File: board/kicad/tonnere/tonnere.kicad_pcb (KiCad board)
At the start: 6 copper layers, 256.2 x 141.3 mm, 403 parts, among them J1 PJ-325C5-G, J10 STM SWD, J12 Conn_01x05, J14 STM USART TTL, J15 SPI CFG, J17 SPI SEL, J18 FPGA GPIO, J19 ESP PGM, J2 PJ-325C5-BL, J20 USB_A, J21 73725-1180RLF, J22 FPGA JTAG, J23 ESP JTAG, J24 CONSOL, J25 73725-1180RLF, J26 73725-1180RLF, J27 I2C, J4 DE15_Pins_HighDensity_Mountin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, J5 HDMI_A, J6 PBI, J7 Conn_01x01, J8 PBI Option, J9 STM GPIO, Q1 BCX51, Q2 DMN2058U, Q3 2N7002, SW1 SA-0-102-C04-0004-WP, SW2 USB HS/FS, U1 TPD4E02B04DQA, U10 TPD8E003DQDR, U11 74LVC1G17, U12 TPD4E02B04DQA, U13 TPD8E003DQDR, U14 TPD8E003DQDR, U15 TPS62903RPJR, U16 TPS62903RPJR, U17 FSUSB42UMX-TP, U18 TPD8E003DQDR, U19 PCM5102A, U2 TPD4E02B04DQA, U20 USB3300-EZK, U21 FSUSB42UMX-TP, U22 TPS62903RPJR, U23 STM32F407ZGTx, U24 TPD8E003DQDR, U25 THS7316DR, U26 PCA9546APWR, U27 M25PX32-VMW, U28 TPD8E003DQDR, U29 M25PX32-VMW, U3 TPD4E02B04DQA, U30 SN74CB3T16211DGVR, U31 IS61WV204816BLL-10BLI, U32 SN74CB3T16211DGVR, U33 10CL040f484, U34 AP2553AW6-7, U35 SN74CB3T16211DGVR, U36 IS61WV204816BLL-10BLI, U37 SN74CB3T16211DGVR, U38 AP2553AW6-7, U39 AP2553AW6-7, U4 TPD4E02B04DQA, U40 ESP32-WROVER-E-N8R8, U41 AP2553AW6-7, U42 AS4C16M16SA, U43 TPD4E02B04DQA, U44 USB2514B_Bi, U45 TPD4E02B04DQA, U46 TPD4E02B04DQA, U47 TPD4E02B04DQA, U5 TPD8E003DQDR, U6 TPD8E003DQDR, U7 TPD8E003DQDR, U8 TPD8E003DQDR, U9 TPD8E003DQDR, Y1 24MHz, Y2 8MHz, Y3 32.768KHz, Y4 25MHz, Y5 Si5351A-B-GT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

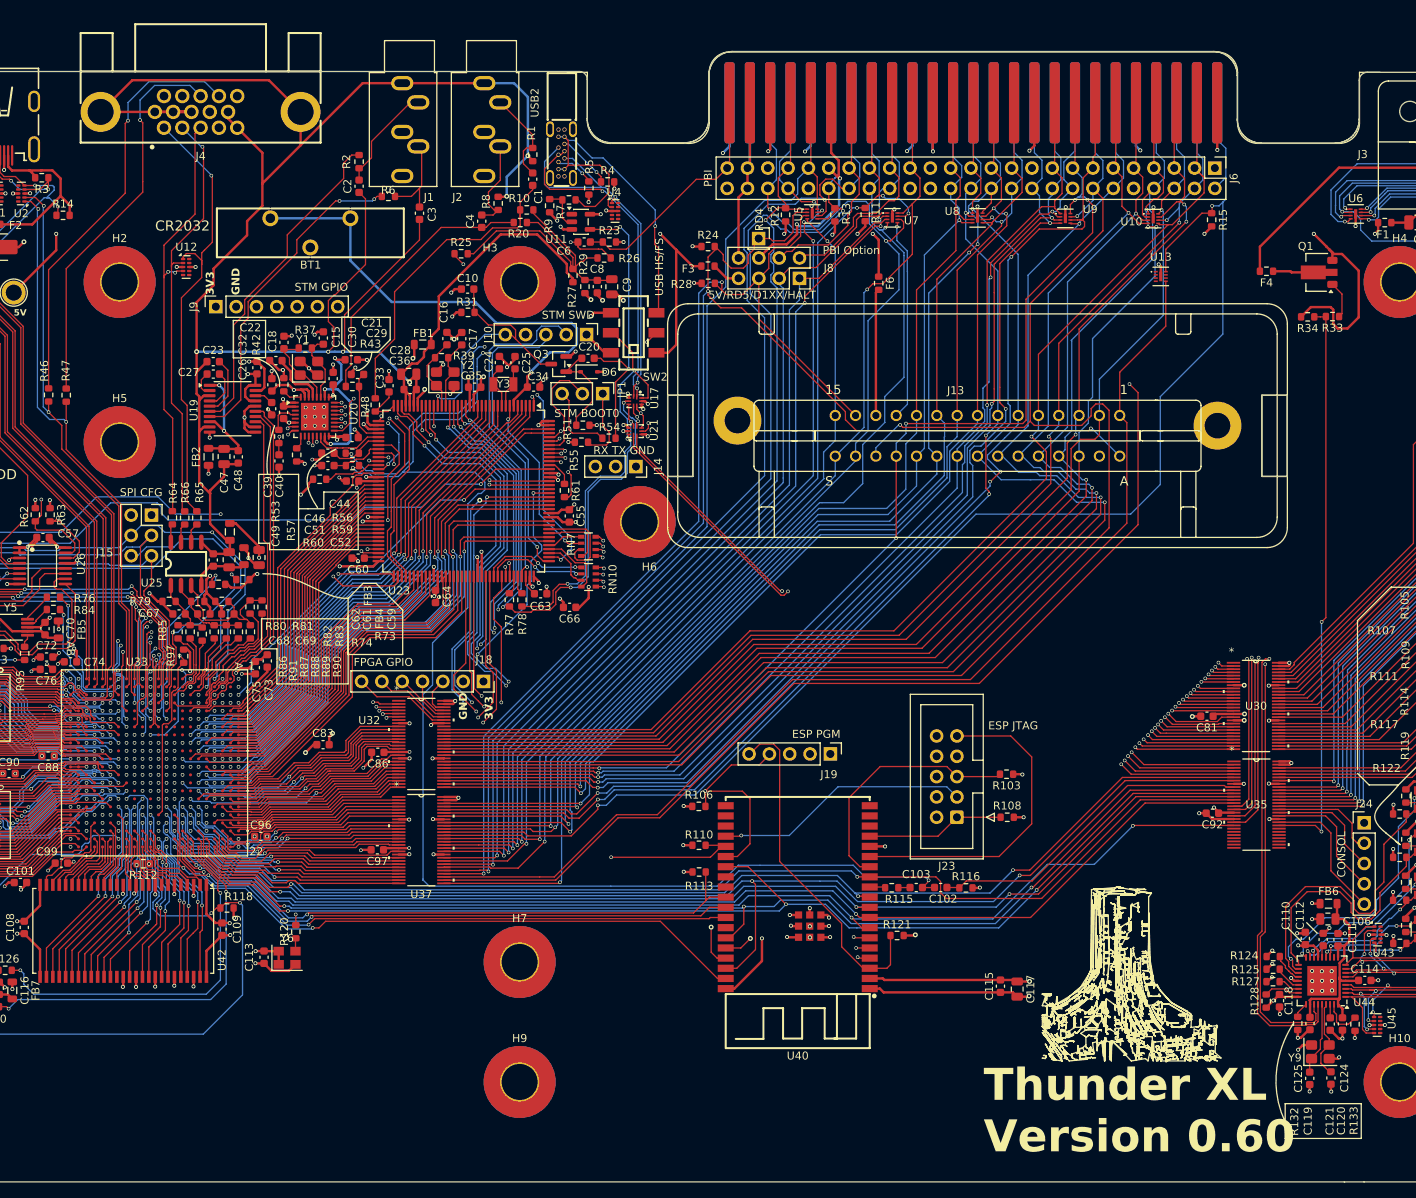
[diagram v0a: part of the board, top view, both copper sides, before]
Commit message: Made audio connector stacked. Added S/PDIF toslink output
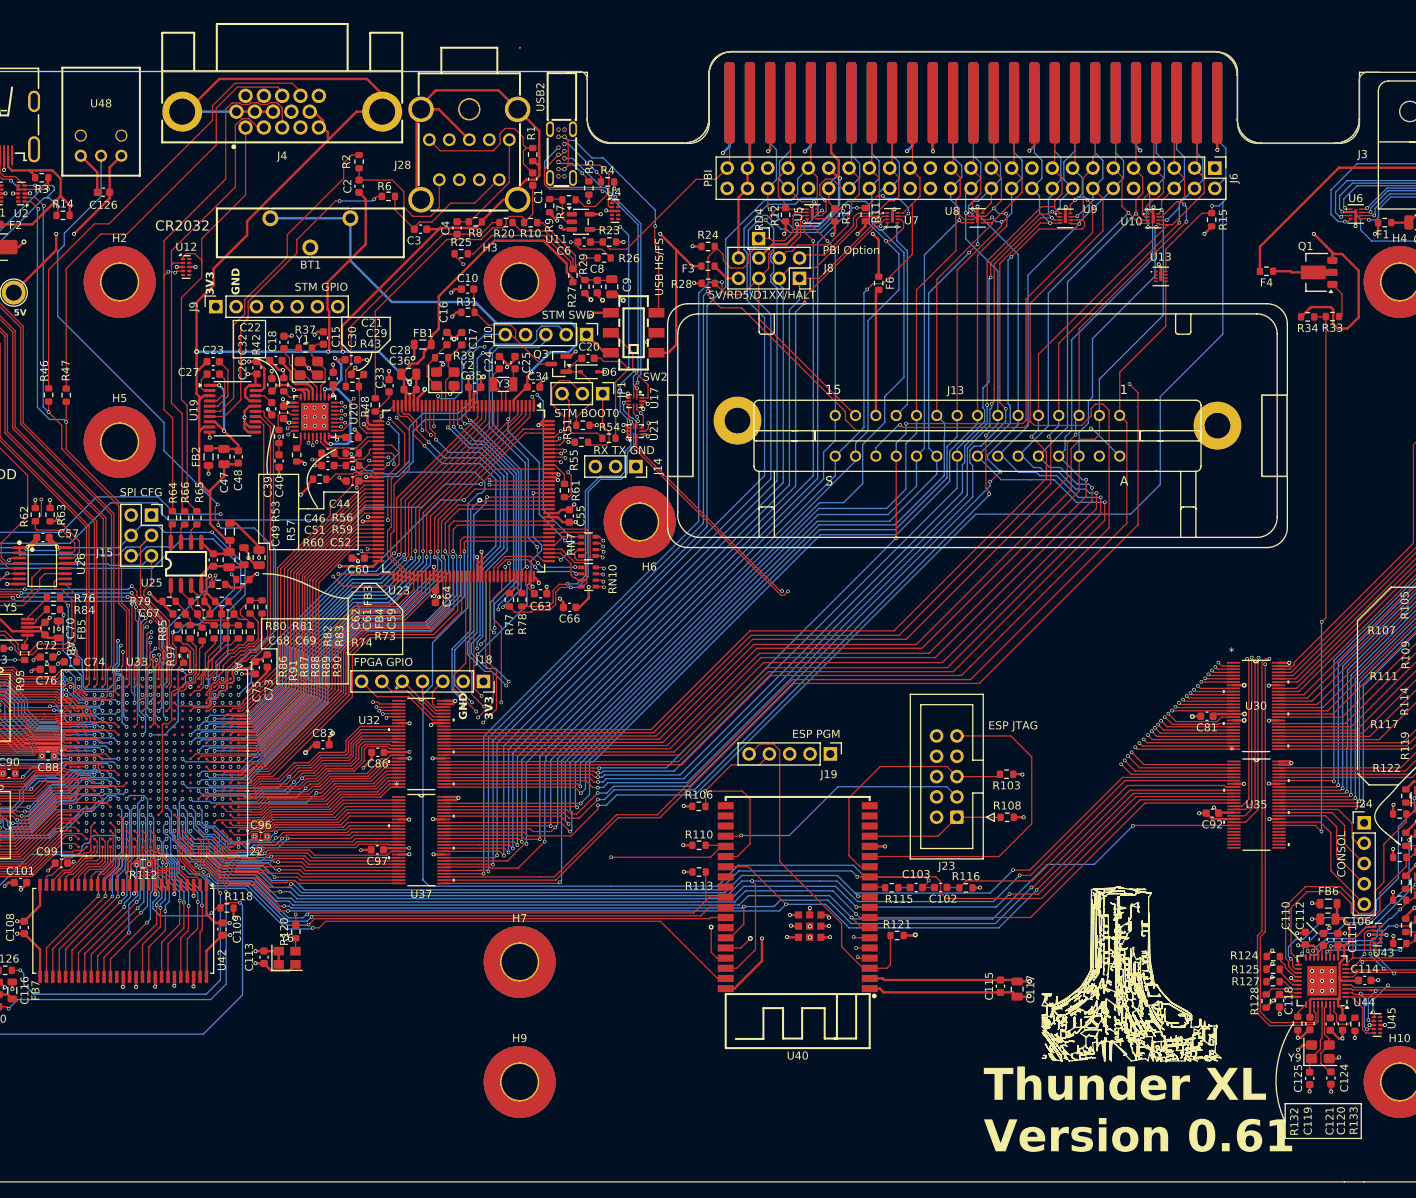
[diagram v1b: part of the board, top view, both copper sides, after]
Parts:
- removed J1: PJ-325C5-G, Connector_Audio:Jack_3.5mm_CUI_SJ1-3535NG_Horizontal
- removed J2: PJ-325C5-BL, Connector_Audio:Jack_3.5mm_CUI_SJ1-3535NG_Horizontal
- added C126: 0.1uF, Capacitor_SMD:C_0603_1608Metric, F.Cu at (59.0, 25.8)
- added J28: JA23331-HA6Q-4F, tonnere:AUDIO-TH_JA23331-HA6Q-4F, F.Cu at (104.7, 21.1)
- added U48: PLT237/T10WH, tonnere:CONN-TH_PLT237-T10WH, F.Cu at (58.7, 20.0)
- moved J4 10.2 mm to (81.3, 15.7)
- moved R8 3.67 mm to (105.5, 29.5), turned to 180 degrees
- moved C4 3.19 mm to (103.2, 30.2)
- moved C3 2.00 mm to (98.6, 30.4), turned to 180 degrees
- moved R20 1.80 mm to (109.3, 29.6)
- moved R10 1.66 mm to (112.4, 29.6)
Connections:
- U33 pad G4: unconnected-(U33A-DIFFIO_L1p-PadG4) -> /Audio/FPGAAUD.SPDIF
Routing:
- net /Audio/FPGAAUD.SPDIF: track 0.00 -> 92.2 mm, vias 0 -> 3
- net /Video/AVID.B: track 53.7 -> 67.7 mm
- net GNDA: track 259.8 -> 272.3 mm, vias 6 -> 4
- net +5V: track 663.9 -> 676.1 mm, vias 17 -> 18
- net Net-(C1-Pad2): track 11.9 -> 20.7 mm
- net Net-(C3-Pad2): track 11.3 -> 18.4 mm
- net Net-(J4-Pad13): track 49.0 -> 55.1 mm, vias 1 -> 0
- net GND: track 536.7 -> 542.2 mm
- net Net-(J4-Pad14): track 53.0 -> 58.2 mm, vias 1 -> 0
- net /Video/AVID.G: track 52.8 -> 57.9 mm, vias 1 -> 0
- net Net-(C2-Pad2): track 13.5 -> 18.5 mm
- net Net-(C4-Pad1): track 34.1 -> 31.7 mm
- net Net-(C4-Pad2): track 11.7 -> 14.0 mm
- net /Video/AVID.R: track 56.4 -> 55.7 mm, vias 1 -> 0
- net Net-(C1-Pad1): track 39.8 -> 40.5 mm
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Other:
- board text added: "Thunder XL Version 0.61"
- board text removed: "Thunder XL Version 0.60"
